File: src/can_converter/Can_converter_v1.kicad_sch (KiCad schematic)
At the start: 18 parts, among them T101 Tab, T102 Tab, T103 Tab, T104 Tab, X1 629722000214_pasteInHole

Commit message: Add jst pa connector, replace tranciever, replace componenets, remove unneeded files
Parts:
- removed NB3, NB4: Passermarke_1mm_1.8mmx1.8mm, mechanical:Passermarke_1mm_1.8mmx1.8mm, symbol mechanical:Passermarke_1mm_1.8mmx1.8mm
- removed T101, T102, T103, T104: Tab, kikit:Tab, symbol kikit:Tab
- removed X2: ~, d-sub:D-SUB-9_side, symbol d-sub:D-SUB-9_side
- added J1: SM02B-PASS, Bluesat:SM02B-PASS, symbol Connector:Conn_01x02_Pin
- R1, R2, R3, R4, R5: footprint Resistor_SMD:R_0402_1005Metric_Pad0.72x0.64mm_HandSolder -> Resistor_SMD:R_0402_1005Metric
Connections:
- new net CAN Transceiver/CAN1_H: J1.2 (Pin_2)
- new net CAN Transceiver/CAN1_L: J1.1 (Pin_1)
- no-connect marks 4 -> 2

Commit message: Finish layout and routing
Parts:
- D1, D2: value KPT-1608SGC -> XL-1608UGC-04; footprint LEDs_Kingbright:LED_Kingbright_0603 -> LED_SMD:LED_0402_1005Metric
- D3: value KPT-1608EC -> XL-1608SURC-06; footprint LEDs_Kingbright:LED_Kingbright_0603 -> LED_SMD:LED_0402_1005Metric
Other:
- moved on the sheet: D1, D2, R3, R4

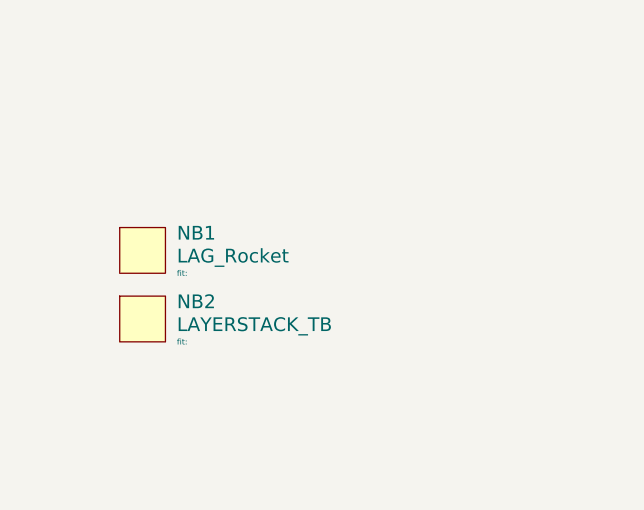
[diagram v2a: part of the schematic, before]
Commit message: Fix silkscreen
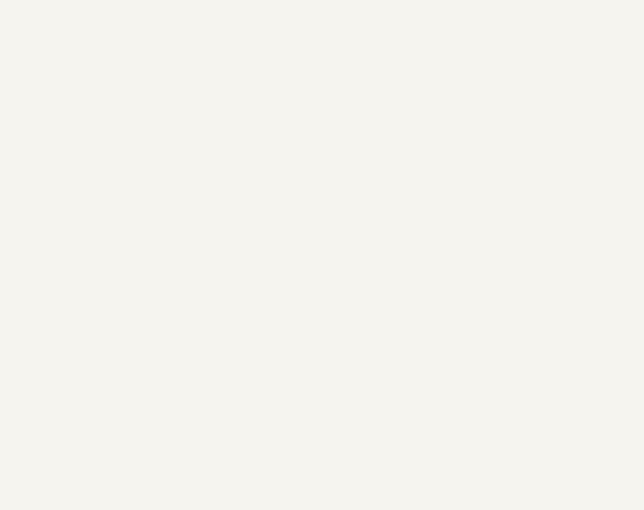
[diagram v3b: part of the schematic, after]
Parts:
- removed NB1: LAG_Rocket, mechanical:lag_rocket_14.5mmx15mm, symbol mechanical:LAG_Rocket
- removed NB2: LAYERSTACK_TB, mechanical:LAYERSTACK_TB, symbol mechanical:LAYERSTACK_TB
- D1, D2, D3: footprint LED_SMD:LED_0402_1005Metric -> LED_SMD:LED_0603_1608Metric
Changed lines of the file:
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@@
-	)
-	(symbol
-		(lib_id "mechanical:LAYERSTACK_TB")
-		(at 26.67 162.56 0)
-		(unit 1)
-		(exclude_from_sim no)
-		(in_bom yes)
-		(on_board yes)
-		(dnp no)
-		(fields_autoplaced yes)
-		(property "Reference" "NB2"
-			(at 30.48 160.655 0)
-			(effects
-				(font
-					(size 1.524 1.524)
-				)
-				(justify left)
-			)
-		)
-		(property "Value" "LAYERSTACK_TB"
-			(at 30.48 163.195 0)
-			(effects
-				(font
-					(size 1.524 1.524)
-				)
-				(justify left)
-			)
-		)
-		(property "Footprint" "mechanical:LAYERSTACK_TB"
-			(at 29.21 167.64 0)
-			(effects
-				(font
-					(size 1.524 1.524)
-				)
-				(hide yes)
-			)
-		)
-		(property "Datasheet" ""
-			(at 26.67 162.56 0)
-			(effects
-				(font
-					(size 1.524 1.524)
-				)
-				(hide yes)
-			)
-		)
-		(property "Description" ""
-			(at 26.67 162.56 0)
-			(effects
-				(font
-					(size 1.27 1.27)
-				)
-			)
-		)
-		(property "Fit" "fit: "
-			(at 30.48 165.1 0)
-			(effects
-				(font
-					(size 0.635 0.635)
-				)
-				(justify left)
-			)
-		)
-		(property "State" "legacy"
-			(at 34.29 166.37 0)
-			(effects
-				(font
-					(size 0.635 0.635)
-				)
-				(hide yes)
-			)
-		)
-		(instances
-			(project "candleLightfd-S01"
-				(path "/e63e39d7-6ac0-4ffd-8aa3-1841a4541b55"
-					(reference "NB2")
-					(unit 1)
-				)
-			)
-		)
 	)
 	(symbol
@@
 			)
 		)
-		(property "Footprint" "LED_SMD:LED_0402_1005Metric"
+		(property "Footprint" "LED_SMD:LED_0603_1608Metric"
 			(at 220.98 128.27 0)
 			(effects
@@
 	)
 	(symbol
-		(lib_id "mechanical:LAG_Rocket")
-		(at 26.67 154.94 0)
-		(unit 1)
-		(exclude_from_sim no)
-		(in_bom yes)
-		(on_board yes)
-		(dnp no)
-		(fields_autoplaced yes)
-		(property "Reference" "NB1"
-			(at 30.48 153.035 0)
-			(effects
-				(font
-					(size 1.524 1.524)
-				)
-				(justify left)
-			)
-		)
-		(property "Value" "LAG_Rocket"
-			(at 30.48 155.575 0)
-			(effects
-				(font
-					(size 1.524 1.524)
-				)
-				(justify left)
-			)
-		)
-		(property "Footprint" "mechanical:lag_rocket_14.5mmx15mm"
-			(at 24.13 153.67 0)
-			(effects
-				(font
-					(size 1.524 1.524)
-				)
-				(hide yes)
-			)
-		)
-		(property "Datasheet" ""
-			(at 26.67 154.94 0)
-			(effects
-				(font
-					(size 1.524 1.524)
-				)
-				(hide yes)
-			)
-		)
-		(property "Description" ""
-			(at 26.67 154.94 0)
-			(effects
-				(font
-					(size 1.27 1.27)
-				)
-			)
-		)
-		(property "Fit" "fit: "
-			(at 30.48 157.48 0)
-			(effects
-				(font
-					(size 0.635 0.635)
-				)
-				(justify left)
-			)
-		)
-		(property "State" "reviewed"
-			(at 34.29 158.75 0)
-			(effects
-				(font
-					(size 0.635 0.635)
-				)
-				(hide yes)
-			)
-		)
-		(instances
-			(project "candleLightfd-S01"
-				(path "/e63e39d7-6ac0-4ffd-8aa3-1841a4541b55"
-					(reference "NB1")
-					(unit 1)
-				)
-			)
-		)
-	)
-	(symbol
 		(lib_id "powerport:+3V3")
 		(at 207.01 114.3 0)
@@
 			)
 		)
-		(property "Footprint" "LED_SMD:LED_0402_1005Metric"
+		(property "Footprint" "LED_SMD:LED_0603_1608Metric"
 			(at 266.7 128.27 0)
 			(effects
@@
 			)
 		)
-		(property "Footprint" "LED_SMD:LED_0402_1005Metric"
+		(property "Footprint" "LED_SMD:LED_0603_1608Metric"
 			(at 243.84 128.27 0)
 			(effects
